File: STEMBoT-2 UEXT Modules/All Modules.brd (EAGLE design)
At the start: 160 x 100 mm, 132 parts, among them IC1 74HC165PW,118, IC2 74HC165PW,118, IC3 74HC165PW,118, J1 FTSH-105-01-XXX-DV-K, J2 FTSH-105-01-XXX-DV-K, J3 FTSH-105-01-XXX-DV-K, J4 FTSH-105-01-XXX-DV-K, J5 FTSH-105-01-XXX-DV-K, J6 FTSH-105-01-XXX-DV-K, Q1 MMBT3904LP-7, Q2 MMBT3904LP-7, Q3 MMBT3904LP-7, U1 TSL260R-LF, U10 SN74HC148D, U11 MAX964ESET, U12 MAX964ESET, U13 HC-SR04(NOSILK), U2 TESEO-LIV3F, U3 CYBLE-012011-00, U4 SN74HC148D, U5 MAX964ESET, U6 MAX964ESET, U7 SN74HC148D, U8 MAX964ESET, U9 MAX964ESET

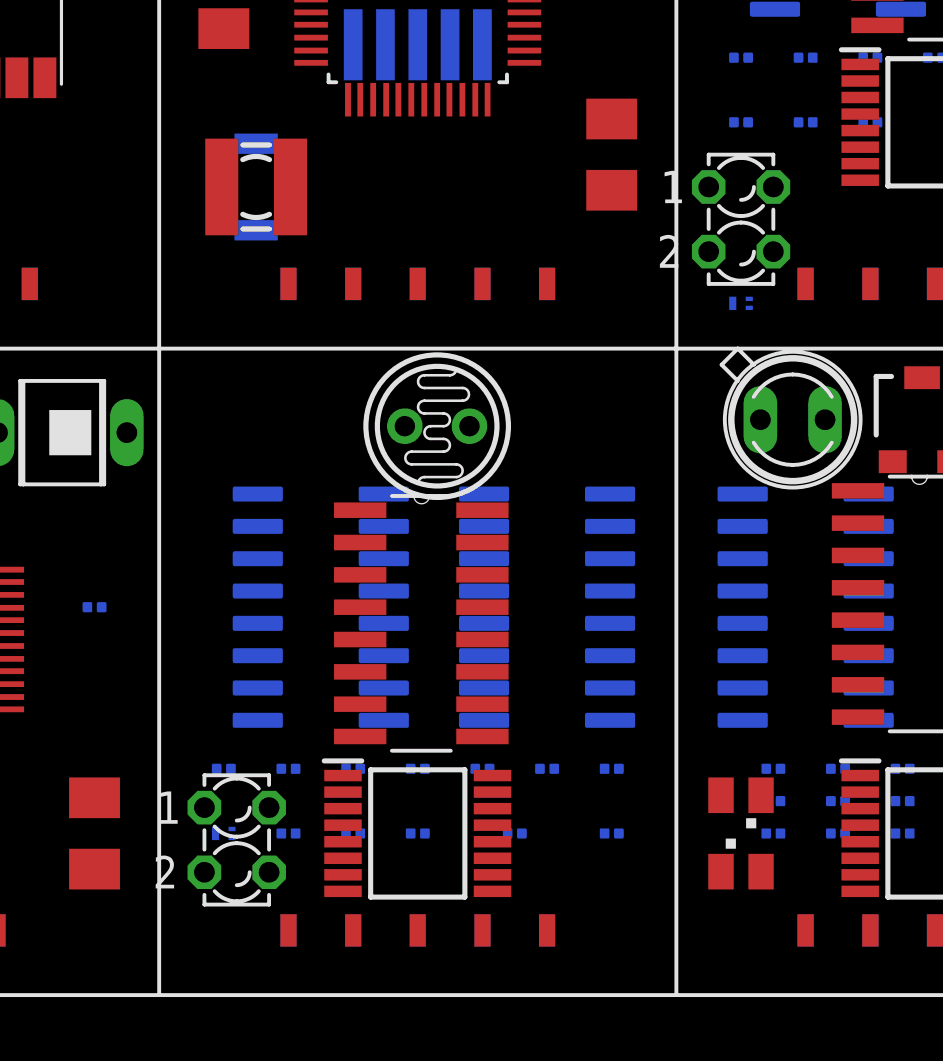
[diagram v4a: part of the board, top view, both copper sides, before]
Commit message: update led footprint
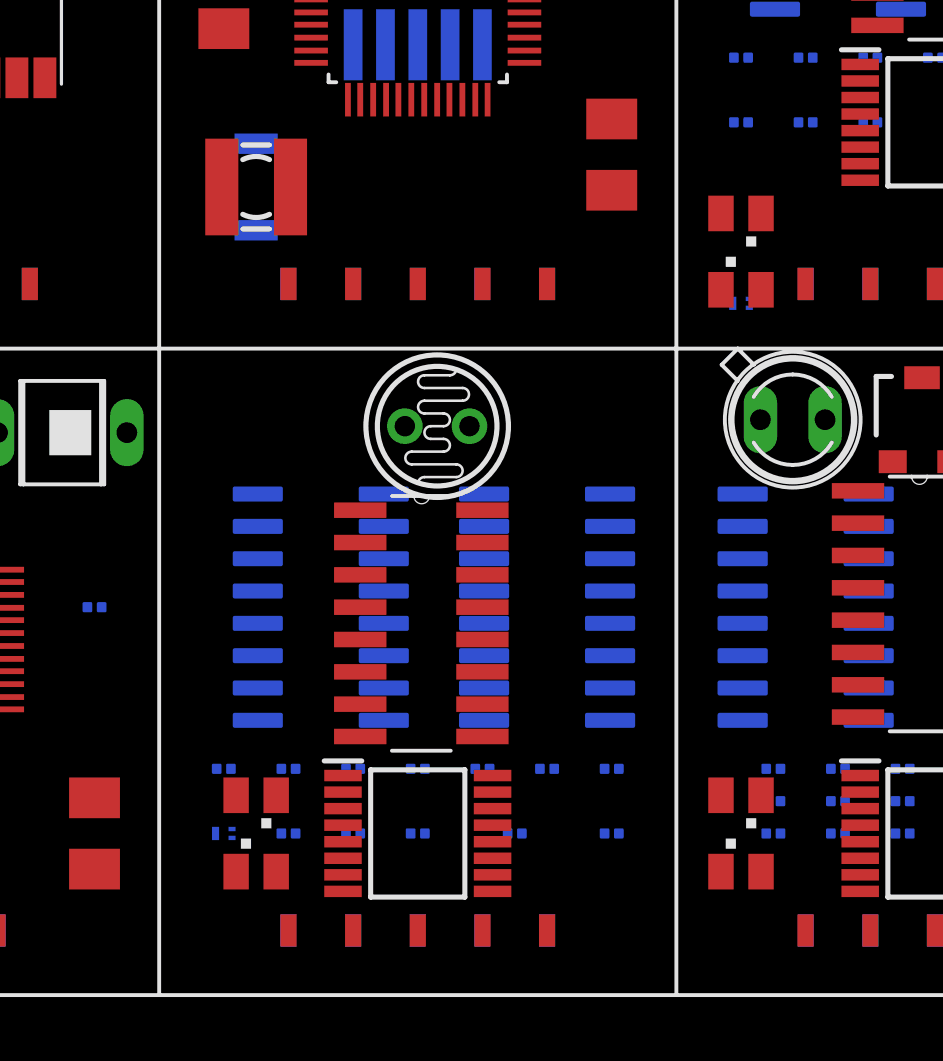
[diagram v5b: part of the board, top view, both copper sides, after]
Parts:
- removed DZ1, DZ2: LZR182, led:LZR182
- added LED10, LED9: LSG-T676, led:P-LCC4-0
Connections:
- net N$10: now also LED10.3; no longer DZ1.K2
- net N$15: now also LED9.3; no longer DZ2.K2
- net N$18: now also LED10.4; no longer DZ1.A2
- net N$39: now also LED10.1; no longer DZ1.K1
- net N$5: now also LED9.2; no longer DZ2.A1
- net N$57: now also LED9.4; no longer DZ2.A2
- net N$64: now also LED9.1; no longer DZ2.K1
- net N$9: now also LED10.2; no longer DZ1.A1
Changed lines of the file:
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@@
 <attribute name="VALUE" x="84.455" y="51.054" size="1.27" layer="27" ratio="10" rot="R180" display="off"/>
-</element>
-<element name="DZ1" library="led" library_urn="urn:adsk.eagle:library:259" package="LZR182" package3d_urn="urn:adsk.eagle:package:15802/1" value="LZR182" x="89.408" y="31.496" smashed="yes">
-<attribute name="NAME" x="88.1126" y="34.2392" size="1.016" layer="25" ratio="10" display="off"/>
-<attribute name="POPULARITY" value="0" x="245.618" y="-607.314" size="1.778" layer="27" display="off"/>
-<attribute name="VALUE" x="92.5322" y="28.702" size="1.016" layer="27" ratio="10" rot="R90" display="off"/>
-</element>
-<element name="DZ2" library="led" library_urn="urn:adsk.eagle:library:259" package="LZR182" package3d_urn="urn:adsk.eagle:package:15802/1" value="LZR182" x="109.22" y="55.88" smashed="yes">
-<attribute name="NAME" x="107.9246" y="58.6232" size="1.016" layer="25" ratio="10" display="off"/>
-<attribute name="POPULARITY" value="0" x="273.05" y="-582.93" size="1.778" layer="27" display="off"/>
-<attribute name="VALUE" x="112.3442" y="53.086" size="1.016" layer="27" ratio="10" rot="R90" display="off"/>
 </element>
 <element name="IC1" library="74HC165PW_118" package="SOP65P640X110-16N" value="74HC165PW,118" x="96.52" y="31.75" smashed="yes">
@@
 <attribute name="PRICE" value="None" x="49.53" y="57.15" size="1.778" layer="28" rot="MR270" display="off"/>
 <attribute name="VALUE" x="52.43" y="59.85" size="1.27" layer="28" rot="MR270" display="off"/>
+</element>
+<element name="LED9" library="led" library_urn="urn:adsk.eagle:library:259" package="P-LCC4-0" package3d_urn="urn:adsk.eagle:package:15893/1" value="LSG-T676" x="109.22" y="54.61" smashed="yes">
+<attribute name="NAME" x="105.41" y="52.07" size="1.27" layer="25" rot="R90" display="off"/>
+<attribute name="POPULARITY" value="0" x="109.22" y="55.88" size="1.778" layer="27" display="off"/>
+<attribute name="VALUE" x="114.3" y="52.07" size="1.27" layer="27" rot="R90" display="off"/>
+</element>
+<element name="LED10" library="led" library_urn="urn:adsk.eagle:library:259" package="P-LCC4-0" package3d_urn="urn:adsk.eagle:package:15893/1" value="LSG-T676" x="90.17" y="31.75" smashed="yes">
+<attribute name="NAME" x="86.36" y="29.21" size="1.27" layer="25" rot="R90" display="off"/>
+<attribute name="POPULARITY" value="0" x="90.17" y="33.02" size="1.778" layer="27" display="off"/>
+<attribute name="VALUE" x="95.25" y="29.21" size="1.27" layer="27" rot="R90" display="off"/>
 </element>
 </elements>
@@
 <wire x1="89.225" y1="31.925" x2="96.24" y2="31.75" width="0" layer="19" extent="16-16"/>
 </signal>
-<signal name="N$9">
-<contactref element="DZ1" pad="A1"/>
-<contactref element="R3" pad="1"/>
-<wire x1="88.138" y1="32.766" x2="100.61" y2="31.75" width="0" layer="19" extent="16-16"/>
-</signal>
 <signal name="N$10">
 <contactref element="Q2" pad="3"/>
-<contactref element="DZ1" pad="K2"/>
-<wire x1="90.678" y1="30.226" x2="88.575" y2="31.75" width="0" layer="19" extent="16-16"/>
+<contactref element="LED10" pad="3"/>
+<wire x1="88.575" y1="31.75" x2="90.9575" y2="33.25" width="0" layer="19" extent="1-16"/>
 </signal>
 <signal name="N$19">
@@
 <signal name="N$18">
 <contactref element="R23" pad="2"/>
-<contactref element="DZ1" pad="A2"/>
-<wire x1="88.138" y1="30.226" x2="88.62" y2="34.29" width="0" layer="19" extent="16-16"/>
+<contactref element="LED10" pad="4"/>
+<wire x1="90.9575" y1="30.25" x2="88.62" y2="34.29" width="0" layer="19" extent="1-16"/>
 </signal>
 <signal name="N$33">
@@
 <contactref element="U$3" pad="2"/>
 <contactref element="IC1" pad="8"/>
-<contactref element="DZ1" pad="K1"/>
 <contactref element="R5" pad="2"/>
 <contactref element="U7" pad="5"/>
+<contactref element="LED10" pad="1"/>
 <wire x1="95.185" y1="37.465" x2="94.2594" y2="39.37" width="0" layer="19" extent="1-16"/>
 <wire x1="94.2594" y1="35.56" x2="95.185" y2="37.465" width="0" layer="19" extent="1-16"/>
@@
 <wire x1="93.582" y1="29.475" x2="93.7" y2="31.75" width="0" layer="19" extent="1-16"/>
 <wire x1="91.44" y1="27.94" x2="93.582" y2="29.475" width="0" layer="19" extent="1-1"/>
-<wire x1="90.678" y1="32.766" x2="93.7" y2="31.75" width="0" layer="19" extent="16-16"/>
-<wire x1="89.225" y1="31.575" x2="90.678" y2="32.766" width="0" layer="19" extent="16-16"/>
+<wire x1="89.3825" y1="30.25" x2="91.44" y2="27.94" width="0" layer="19" extent="1-1"/>
+<wire x1="89.225" y1="31.575" x2="89.3825" y2="30.25" width="0" layer="19" extent="1-16"/>
 <wire x1="90.235" y1="40.005" x2="94.2594" y2="39.37" width="0" layer="19" extent="1-16"/>
 </signal>
@@
 <wire x1="109.545" y1="52.753" x2="111.48" y2="59.69" width="0" layer="19" extent="16-16"/>
 </signal>
-<signal name="N$5">
-<contactref element="DZ2" pad="A1"/>
-<contactref element="R30" pad="1"/>
-<wire x1="107.95" y1="57.15" x2="109.5" y2="62.23" width="0" layer="19" extent="16-16"/>
-</signal>
 <signal name="N$15">
 <contactref element="Q3" pad="3"/>
-<contactref element="DZ2" pad="K2"/>
-<wire x1="108.895" y1="52.578" x2="110.49" y2="54.61" width="0" layer="19" extent="16-16"/>
+<contactref element="LED9" pad="3"/>
+<wire x1="108.895" y1="52.578" x2="110.0075" y2="56.11" width="0" layer="19" extent="1-16"/>
 </signal>
 <signal name="N$17">
@@
 <signal name="N$57">
 <contactref element="R40" pad="2"/>
-<contactref element="DZ2" pad="A2"/>
-<wire x1="107.95" y1="54.61" x2="108.94" y2="59.69" width="0" layer="19" extent="16-16"/>
+<contactref element="LED9" pad="4"/>
+<wire x1="110.0075" y1="53.11" x2="108.94" y2="59.69" width="0" layer="19" extent="1-16"/>
 </signal>
 <signal name="N$58">
@@
 <contactref element="U$2" pad="2"/>
 <contactref element="IC2" pad="8"/>
-<contactref element="DZ2" pad="K1"/>
 <contactref element="R20" pad="1A"/>
 <contactref element="U10" pad="5"/>
+<contactref element="LED9" pad="1"/>
 <wire x1="114.5794" y1="67.31" x2="120.57" y2="73.51" width="0" layer="19" extent="1-1"/>
 <wire x1="115.505" y1="65.405" x2="114.5794" y2="67.31" width="0" layer="19" extent="1-16"/>
@@
 <wire x1="110.555" y1="67.945" x2="114.5794" y2="67.31" width="0" layer="19" extent="1-16"/>
 <wire x1="113.902" y1="57.415" x2="114.58" y2="62.23" width="0" layer="19" extent="1-16"/>
-<wire x1="110.49" y1="57.15" x2="113.902" y2="57.415" width="0" layer="19" extent="1-1"/>
-<wire x1="111.76" y1="53.34" x2="110.49" y2="57.15" width="0" layer="19" extent="1-1"/>
+<wire x1="111.76" y1="53.34" x2="113.902" y2="57.415" width="0" layer="19" extent="1-1"/>
 <wire x1="109.545" y1="52.403" x2="111.76" y2="53.34" width="0" layer="19" extent="1-16"/>
+<wire x1="108.4325" y1="53.11" x2="109.545" y2="52.403" width="0" layer="19" extent="1-16"/>
 </signal>
 <signal name="N$65">
@@
 <wire x1="93.582" y1="34.025" x2="99.06" y2="27.94" width="0" layer="19" extent="1-1"/>
 </signal>
+<signal name="N$5">
+<contactref element="R30" pad="1"/>
+<contactref element="LED9" pad="2"/>
+<wire x1="108.4325" y1="56.11" x2="109.5" y2="62.23" width="0" layer="19" extent="1-16"/>
+</signal>
+<signal name="N$9">
+<contactref element="R3" pad="1"/>
+<contactref element="LED10" pad="2"/>
+<wire x1="89.3825" y1="33.25" x2="100.61" y2="31.75" width="0" layer="19" extent="1-16"/>
+</signal>
 </signals>

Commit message: final pcb board layout for reveiw
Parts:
- added R56, R59, R60: ERJ-1RHD3601C, Resistor:RESC0603X26N
- moved R9 17.1 mm to (114.9, 48.3), turned to 270 degrees
- moved R10 17.1 mm to (117.5, 48.3), turned to 270 degrees
- moved R55 16.6 mm to (40.6, 71.1), turned to 270 degrees
- moved R14 14.1 mm to (116.2, 48.3)
- moved Q1 14.0 mm to (109.2, 31.1)
- moved R29 13.0 mm to (124.5, 59.7)
- moved R13 9.94 mm to (111.8, 29.8), turned to 180 degrees
- moved R1 9.53 mm to (112.4, 59.7)
- moved R24 9.25 mm to (115.6, 59.7), turned to 180 degrees
- moved R30 8.89 mm to (109.2, 53.3), turned to 180 degrees
- moved R4 8.03 mm to (88.9, 29.2)
- moved R23 6.35 mm to (88.9, 27.9)
- moved R27 6.29 mm to (112.4, 57.8), turned to 180 degrees
- moved R12 5.43 mm to (123.2, 29.8)
- moved R37 5.12 mm to (120.7, 32.4)
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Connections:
- removed net N$145: IC2.1, U$2.8
- removed net N$159: R61.1
- removed net N$163: IC3.1, U$1.8
- removed net N$2: U1.3
- new net N$158: IC3.1, R56.1, U$1.8
- new net N$164: IC2.1, R60.1, U$2.8
- net N$100: now also U4.13; no longer U4.1
- net N$125: now also U1.3
- net N$157: now also R61.1
- net N$162: now also R59.1
- net N$20: no longer IC1.10
- net N$39: now also IC1.14, IC1.3, IC1.4, IC1.5, IC1.6, R59.2
- net N$43: now also U7.1; no longer U7.13
- net N$44: now also U7.13; no longer U7.1
- net N$53: no longer IC2.10
- net N$55: now also R56.2
- net N$64: now also IC2.14, IC2.3, IC2.4, IC2.5, IC2.6, R60.2
- net N$68: now also U10.1; no longer U10.13
- net N$69: now also U10.13; no longer U10.1
- net N$99: now also U4.1; no longer U4.13
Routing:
- net N$55: track 0.00 -> 118.9 mm, vias 0 -> 20
- net N$144: track 0.00 -> 91.9 mm, vias 0 -> 11
- net N$161: track 0.00 -> 83.5 mm, vias 0 -> 10
- net N$39: track 0.00 -> 78.3 mm, vias 0 -> 10
- net N$108: track 0.00 -> 76.9 mm, vias 0 -> 9
- net N$138: track 0.00 -> 76.6 mm, vias 0 -> 9
- net N$64: track 0.00 -> 75.5 mm, vias 0 -> 9
- net N$79: track 0.00 -> 75.2 mm, vias 0 -> 9
- net N$12: track 0.00 -> 74.7 mm, vias 0 -> 7
- net N$51: track 0.00 -> 73.8 mm, vias 0 -> 7
- net N$109: track 0.00 -> 70.5 mm, vias 0 -> 5
- net N$113: track 0.00 -> 70.5 mm, vias 0 -> 11
- net N$137: track 0.00 -> 69.2 mm, vias 0 -> 8
- net N$119: track 0.00 -> 67.4 mm, vias 0 -> 7
- net N$1: track 0.00 -> 66.2 mm, vias 0 -> 9
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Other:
- board size 160 x 100 mm -> 105.4 x 54.9 mm
- board text added: "Bluetooth Module"
- board text added: "Capstone Team 8"
- board text added: "GPS Module"
- board text added: "Infared Proximity Module"
- board text added: "Infared Remote Module"
- board text added: "Photoresistor Module"
- board text added: "Potentiometer Module"
- board text added: "Ultrasonic Module"

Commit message: I am a little wary off all this stuff in here. I went ahead and added an ultrasonic schem in here. Dont know why it wasnt in before.
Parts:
- removed R14: ERJ-1RHD3601C, Resistor:RESC0603X26N
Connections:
- removed net N$70: D2.A, R10.2
- removed net N$79: R14.2, U5.2, U5.4, U5.6, U5.8, U6.2, U6.4, U6.6, U6.8
- new net N$145: R39.1, VR1.2
- new net N$2: D1.A, D2.K, IC3.16, R11.1, R12.2, U$1.1, U4.16, U5.13, U6.13, VR1.3
- net N$55: no longer D1.A, D2.K, IC3.16, R11.1, R12.2, R39.1, U$1.1, U4.16, U5.13, U6.13, VR1.3
- net N$71: now also D2.A, R10.2, U5.2, U5.4, U5.6, U5.8, U6.2, U6.4, U6.6, U6.8; no longer R14.1, VR1.2
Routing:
- net N$79: track 75.2 -> 0.00 mm, vias 9 -> 0
- net N$71: track 3.85 -> 77.5 mm, vias 1 -> 10
- net N$55: track 118.9 -> 103.2 mm
- net N$145: track 0.00 -> 3.65 mm, vias 0 -> 1
- net N$70: track 2.64 -> 0.00 mm, vias 1 -> 0

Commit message: final board design and generated gerber files
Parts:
- moved R39 14.5 mm to (116.2, 47.0), turned to 180 degrees
- moved LED8 0.63 mm to (109.2, 30.5)
- moved Q1 0.63 mm to (109.2, 30.5)
- moved R11 0.63 mm to (110.5, 31.8)
- moved R56 0.63 mm to (107.8, 29.7)
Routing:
- net N$2: track 0.00 -> 78.7 mm, vias 0 -> 8
- net N$80: track 16.0 -> 26.8 mm, vias 2 -> 3
- net N$55: track 103.2 -> 94.6 mm, vias 20 -> 16
- net N$145: track 3.65 -> 5.88 mm
- net N$71: track 77.5 -> 78.9 mm
- net N$32: track 3.37 -> 4.66 mm
- net N$89: track 14.6 -> 15.5 mm
- net N$158: track 31.2 -> 31.9 mm
- net N$92: track 24.3 -> 24.9 mm
- net N$72: track 3.08 -> 3.59 mm
